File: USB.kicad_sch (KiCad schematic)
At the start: 10 parts, among them IC5 ADuM4160

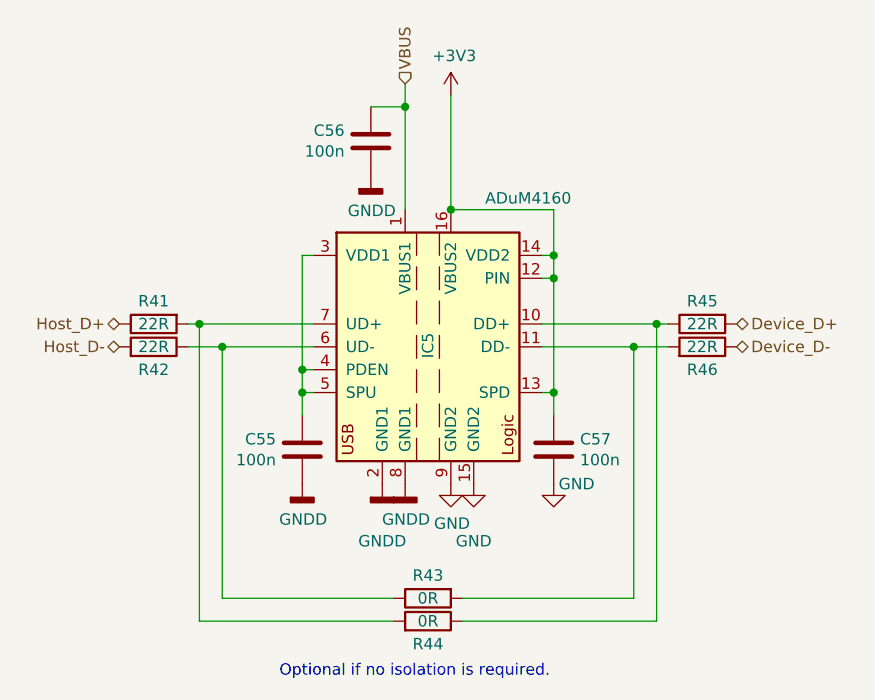
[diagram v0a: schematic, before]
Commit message: - peeled back the filler planes around HV logic - improved insulation on HV logic
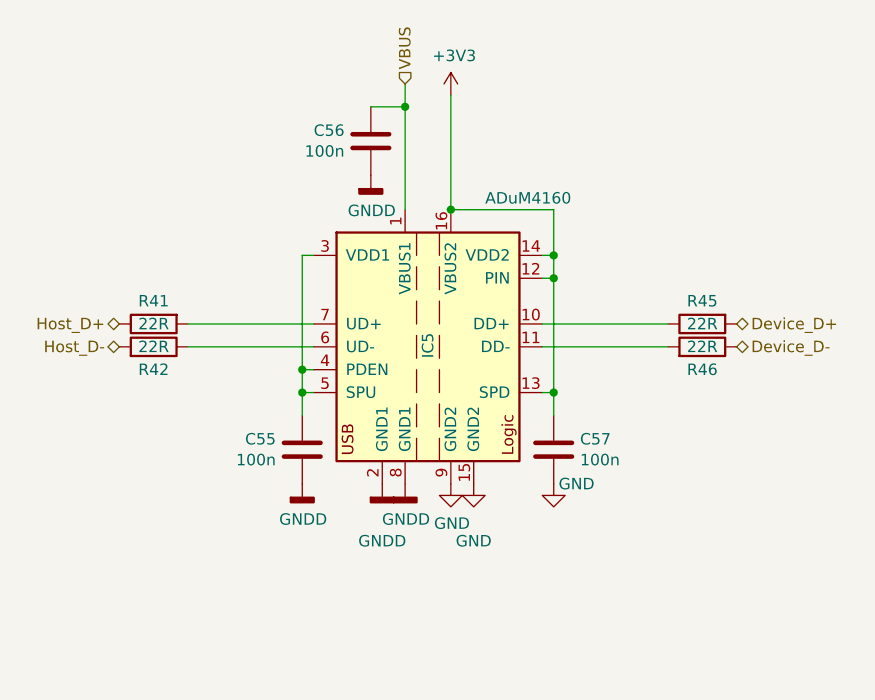
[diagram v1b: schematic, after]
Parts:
- removed R43, R44: 0R, Resistor_SMD:R_0805_2012Metric, symbol Device:R
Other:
- note removed: "Optional if no isolation is required."
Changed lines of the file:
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@@
   (junction (at 158.75 87.63) (diameter 0) (color 0 0 0 0)
   )
-  (junction (at 170.18 92.71) (diameter 0) (color 0 0 0 0)
-  )
   (junction (at 158.75 85.09) (diameter 0) (color 0 0 0 0)
   )
   (junction (at 147.32 80.01) (diameter 0) (color 0 0 0 0)
   )
-  (junction (at 119.38 92.71) (diameter 0) (color 0 0 0 0)
-  )
   (junction (at 158.75 100.33) (diameter 0) (color 0 0 0 0)
   )
@@
   (junction (at 130.81 97.79) (diameter 0) (color 0 0 0 0)
   )
-  (junction (at 121.92 95.25) (diameter 0) (color 0 0 0 0)
-  )
-  (junction (at 167.64 95.25) (diameter 0) (color 0 0 0 0)
-  )
   (wire (pts (xy 158.75 100.33) (xy 158.75 102.87))
     (stroke (width 0) (type default))
   )
-  (wire (pts (xy 167.64 95.25) (xy 157.48 95.25))
-    (stroke (width 0) (type default))
-  )
-  (wire (pts (xy 121.92 95.25) (xy 132.08 95.25))
-    (stroke (width 0) (type default))
-  )
-  (wire (pts (xy 170.18 125.73) (xy 170.18 92.71))
-    (stroke (width 0) (type default))
-  )
-  (wire (pts (xy 119.38 92.71) (xy 118.11 92.71))
+  (wire (pts (xy 118.11 92.71) (xy 132.08 92.71))
     (stroke (width 0) (type default))
   )
@@
     (stroke (width 0) (type default))
   )
-  (wire (pts (xy 140.97 123.19) (xy 121.92 123.19))
-    (stroke (width 0) (type default))
-  )
   (wire (pts (xy 147.32 80.01) (xy 158.75 80.01))
     (stroke (width 0) (type default))
   )
-  (wire (pts (xy 171.45 92.71) (xy 170.18 92.71))
-    (stroke (width 0) (type default))
-  )
   (wire (pts (xy 130.81 85.09) (xy 132.08 85.09))
     (stroke (width 0) (type default))
   )
-  (wire (pts (xy 171.45 95.25) (xy 167.64 95.25))
+  (wire (pts (xy 157.48 95.25) (xy 171.45 95.25))
     (stroke (width 0) (type default))
   )
@@
     (stroke (width 0) (type default))
   )
-  (wire (pts (xy 148.59 123.19) (xy 167.64 123.19))
-    (stroke (width 0) (type default))
-  )
-  (wire (pts (xy 119.38 92.71) (xy 119.38 125.73))
-    (stroke (width 0) (type default))
-  )
-  (wire (pts (xy 132.08 92.71) (xy 119.38 92.71))
-    (stroke (width 0) (type default))
-  )
   (wire (pts (xy 147.32 67.31) (xy 147.32 80.01))
     (stroke (width 0) (type default))
   )
-  (wire (pts (xy 170.18 92.71) (xy 157.48 92.71))
+  (wire (pts (xy 157.48 92.71) (xy 171.45 92.71))
     (stroke (width 0) (type default))
   )
@@
     (stroke (width 0) (type default))
   )
-  (wire (pts (xy 118.11 95.25) (xy 121.92 95.25))
-    (stroke (width 0) (type default))
-  )
-  (wire (pts (xy 148.59 125.73) (xy 170.18 125.73))
-    (stroke (width 0) (type default))
-  )
-  (wire (pts (xy 121.92 123.19) (xy 121.92 95.25))
+  (wire (pts (xy 118.11 95.25) (xy 132.08 95.25))
     (stroke (width 0) (type default))
   )
@@
   (wire (pts (xy 157.48 100.33) (xy 158.75 100.33))
     (stroke (width 0) (type default))
-  )
-  (wire (pts (xy 167.64 123.19) (xy 167.64 95.25))
-    (stroke (width 0) (type default))
-  )
-  (wire (pts (xy 119.38 125.73) (xy 140.97 125.73))
-    (stroke (width 0) (type default))
-  )
-  (text "Optional if no isolation is required." (at 128.27 132.08 0)
-    (effects (font (size 1.27 1.27)) (justify left bottom))
   )
   (hierarchical_label "Host_D-" (shape bidirectional) (at 110.49 95.25 180) (fields_autoplaced)
@@
         )
       )
-    )
-  )
-  (symbol (lib_id "Device:R") (at 144.78 125.73 270) (mirror x) (unit 1)
-    (in_bom yes) (on_board yes) (dnp no)
-    (property "Reference" "R44" (at 144.78 128.27 90)
-      (effects (font (size 1.27 1.27)))
-    )
-    (property "Value" "0R" (at 144.78 125.73 90)
-      (effects (font (size 1.27 1.27)))
-    )
-    (property "Footprint" "Resistor_SMD:R_0805_2012Metric" (at 144.78 127.508 90)
-      (effects (font (size 1.27 1.27)) hide)
-    )
-    (property "Datasheet" "~" (at 144.78 125.73 0)
-      (effects (font (size 1.27 1.27)) hide)
-    )
-    (pin "1")
-    (pin "2")
-    (instances
-      (project "HSWR"
-        (path "/51094070-255e-40e7-bed5-d199e288e5dd/00000000-0000-0000-0000-00005ca14308"
-          (reference "R44") (unit 1)
-        )
-      )
-    )
-  )
-  (symbol (lib_id "Device:R") (at 144.78 123.19 90) (mirror x) (unit 1)
-    (in_bom yes) (on_board yes) (dnp no)
-    (property "Reference" "R43" (at 144.78 120.65 90)
-      (effects (font (size 1.27 1.27)))
-    )
-    (property "Value" "0R" (at 144.78 123.19 90)
-      (effects (font (size 1.27 1.27)))
-    )
-    (property "Footprint" "Resistor_SMD:R_0805_2012Metric" (at 144.78 121.412 90)
-      (effects (font (size 1.27 1.27)) hide)
-    )
-    (property "Datasheet" "~" (at 144.78 123.19 0)
-      (effects (font (size 1.27 1.27)) hide)
-    )
-    (pin "1")
-    (pin "2")
-    (instances
-      (project "HSWR"
-        (path "/51094070-255e-40e7-bed5-d199e288e5dd/00000000-0000-0000-0000-00005ca14308"
-          (reference "R43") (unit 1)
-        )
-      )
